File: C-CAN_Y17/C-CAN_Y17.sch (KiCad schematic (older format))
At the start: 19 parts, among them P3 CAN_Terminate, P4 MX150_8, P5 MX150_16, SW1 SW_Push, U1 MCP2551-I/SN, U2 AP1117, U3 Cypress_5LP, Y1 Crystal

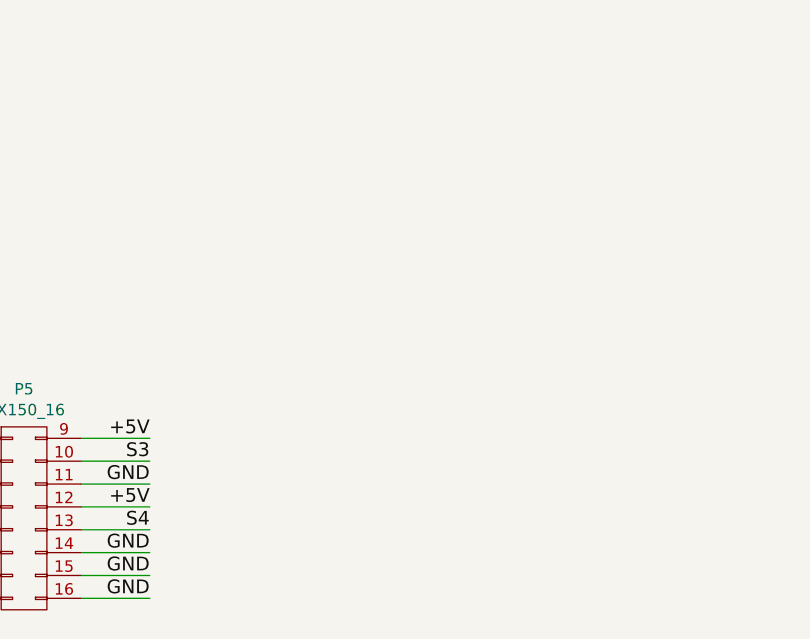
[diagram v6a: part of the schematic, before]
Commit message: C-CAN_Y17 Layout done, Oshpark DRC compliant
Still need to do the BOM but everything on the KiCAD side is complete
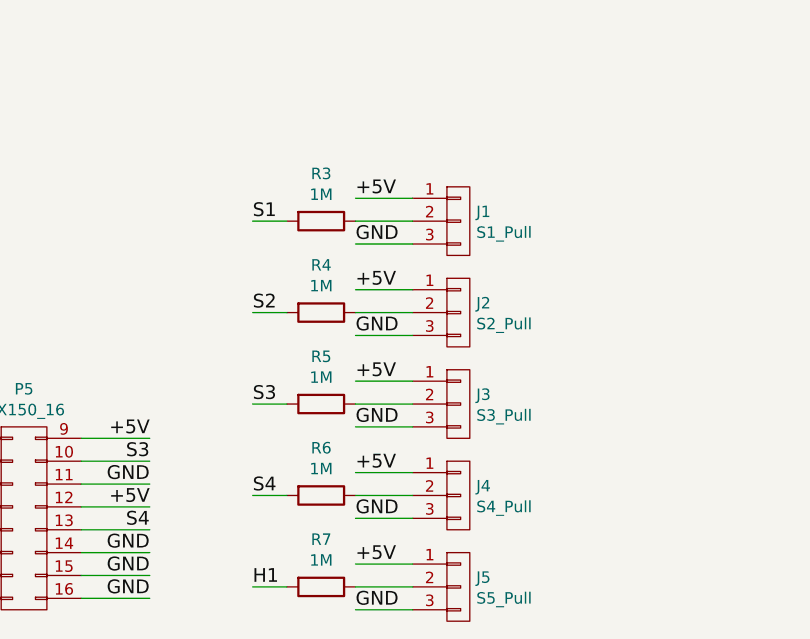
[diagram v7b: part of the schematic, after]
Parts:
- added J1: S1_Pull, Pin_Headers:Pin_Header_Straight_1x03_Pitch2.54mm, symbol CONN_01X03
- added J2: S2_Pull, Pin_Headers:Pin_Header_Straight_1x03_Pitch2.54mm, symbol CONN_01X03
- added J3: S3_Pull, Pin_Headers:Pin_Header_Straight_1x03_Pitch2.54mm, symbol CONN_01X03
- added J4: S4_Pull, Pin_Headers:Pin_Header_Straight_1x03_Pitch2.54mm, symbol CONN_01X03
- added J5: S5_Pull, Pin_Headers:Pin_Header_Straight_1x03_Pitch2.54mm, symbol CONN_01X03
- added R3, R4, R5, R6, R7: 1M, Resistors_SMD:R_0805_HandSoldering, symbol R
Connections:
- net +5V: now also J1.1 (P1), J2.1 (P1), J3.1 (P1), J4.1 (P1), J5.1 (P1)
- net GND: now also J1.3 (P3), J2.3 (P3), J3.3 (P3), J4.3 (P3), J5.3 (P3)
- net H1: now also R7.2
- net S1: now also R3.2
- net S2: now also R4.2
- net S3: now also R5.2
- net S4: now also R6.2
- new net: J1.2 (P2), R3.1
- new net: J2.2 (P2), R4.1
- new net: J3.2 (P2), R5.1
- new net: J4.2 (P2), R6.1
- new net: J5.2 (P2), R7.1
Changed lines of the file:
@@
 $EndComp
 Connection ~ 2700 1450
+$Comp
+L CONN_01X03 J1
+U 1 1 58BF3A96
+P 5300 5150
+F 0 "J1" H 5378 5191 50  0000 L CNN
+F 1 "S1_Pull" H 5378 5100 50  0000 L CNN
+F 2 "Pin_Headers:Pin_Header_Straight_1x03_Pitch2.54mm" H 850 -1250 50  0001 C CNN
+F 3 "" H 850 -1250 50  0001 C CNN
+	1    5300 5150
+	1    0    0    -1
+$EndComp
+$Comp
+L CONN_01X03 J2
+U 1 1 58BF3AFC
+P 5300 5550
+F 0 "J2" H 5378 5591 50  0000 L CNN
+F 1 "S2_Pull" H 5378 5500 50  0000 L CNN
+F 2 "Pin_Headers:Pin_Header_Straight_1x03_Pitch2.54mm" H 0   0   50  0001 C CNN
+F 3 "" H 0   0   50  0001 C CNN
+	1    5300 5550
+	1    0    0    -1
+$EndComp
+$Comp
+L CONN_01X03 J3
+U 1 1 58BF3B4E
+P 5300 5950
+F 0 "J3" H 5378 5991 50  0000 L CNN
+F 1 "S3_Pull" H 5378 5900 50  0000 L CNN
+F 2 "Pin_Headers:Pin_Header_Straight_1x03_Pitch2.54mm" H 50  0   50  0001 C CNN
+F 3 "" H 50  0   50  0001 C CNN
+	1    5300 5950
+	1    0    0    -1
+$EndComp
+$Comp
+L CONN_01X03 J4
+U 1 1 58BF3BA4
+P 5300 6350
+F 0 "J4" H 5378 6391 50  0000 L CNN
+F 1 "S4_Pull" H 5378 6300 50  0000 L CNN
+F 2 "Pin_Headers:Pin_Header_Straight_1x03_Pitch2.54mm" H 0   -50 50  0001 C CNN
+F 3 "" H 0   -50 50  0001 C CNN
+	1    5300 6350
+	1    0    0    -1
+$EndComp
+$Comp
+L CONN_01X03 J5
+U 1 1 58BF3BFC
+P 5300 6750
+F 0 "J5" H 5378 6791 50  0000 L CNN
+F 1 "S5_Pull" H 5378 6700 50  0000 L CNN
+F 2 "Pin_Headers:Pin_Header_Straight_1x03_Pitch2.54mm" H 0   -50 50  0001 C CNN
+F 3 "" H 0   -50 50  0001 C CNN
+	1    5300 6750
+	1    0    0    -1
+$EndComp
+Text Label 4850 5050 0    60   ~ 0
++5V
+Text Label 4850 5450 0    60   ~ 0
++5V
+Text Label 4850 5850 0    60   ~ 0
++5V
+Text Label 4850 6250 0    60   ~ 0
++5V
+Text Label 4850 6650 0    60   ~ 0
++5V
+Text Label 4850 5250 0    60   ~ 0
+GND
+Text Label 4850 5650 0    60   ~ 0
+GND
+Text Label 4850 6050 0    60   ~ 0
+GND
+Text Label 4850 6450 0    60   ~ 0
+GND
+Text Label 4850 6850 0    60   ~ 0
+GND
+Text Label 4400 5150 0    60   ~ 0
+S1
+Text Label 4400 5550 0    60   ~ 0
+S2
+Text Label 4400 5950 0    60   ~ 0
+S3
+Text Label 4400 6350 0    60   ~ 0
+S4
+Text Label 4400 6750 0    60   ~ 0
+H1
+$Comp
+L R R3
+U 1 1 58BF40AB
+P 4700 5150
+F 0 "R3" V 4493 5150 50  0000 C CNN
+F 1 "1M" V 4584 5150 50  0000 C CNN
+F 2 "Resistors_SMD:R_0805_HandSoldering" V 630 -350 50  0001 C CNN
+F 3 "" H 700 -350 50  0001 C CNN
+	1    4700 5150
+	0    1    1    0
+$EndComp
+$Comp
+L R R4
+U 1 1 58BF4147
+P 4700 5550
+F 0 "R4" V 4493 5550 50  0000 C CNN
+F 1 "1M" V 4584 5550 50  0000 C CNN
+F 2 "Resistors_SMD:R_0805_HandSoldering" V 130 0   50  0001 C CNN
+F 3 "" H 200 0   50  0001 C CNN
+	1    4700 5550
+	0    1    1    0
+$EndComp
+$Comp
+L R R5
+U 1 1 58BF41C2
+P 4700 5950
+F 0 "R5" V 4493 5950 50  0000 C CNN
+F 1 "1M" V 4584 5950 50  0000 C CNN
+F 2 "Resistors_SMD:R_0805_HandSoldering" V 130 0   50  0001 C CNN
+F 3 "" H 200 0   50  0001 C CNN
+	1    4700 5950
+	0    1    1    0
+$EndComp
+$Comp
+L R R6
+U 1 1 58BF42C4
+P 4700 6350
+F 0 "R6" V 4493 6350 50  0000 C CNN
+F 1 "1M" V 4584 6350 50  0000 C CNN
+F 2 "Resistors_SMD:R_0805_HandSoldering" V 130 0   50  0001 C CNN
+F 3 "" H 200 0   50  0001 C CNN
+	1    4700 6350
+	0    1    1    0
+$EndComp
+$Comp
+L R R7
+U 1 1 58BF4345
+P 4700 6750
+F 0 "R7" V 4493 6750 50  0000 C CNN
+F 1 "1M" V 4584 6750 50  0000 C CNN
+F 2 "Resistors_SMD:R_0805_HandSoldering" V 130 0   50  0001 C CNN
+F 3 "" H 200 0   50  0001 C CNN
+	1    4700 6750
+	0    1    1    0
+$EndComp
+Wire Wire Line
+	4400 5150 4550 5150
+Wire Wire Line
+	4400 5550 4550 5550
+Wire Wire Line
+	4400 5950 4550 5950
+Wire Wire Line
+	4400 6350 4550 6350
+Wire Wire Line
+	4400 6750 4550 6750
+Wire Wire Line
+	4850 5150 5100 5150
+Wire Wire Line
+	4850 5050 5100 5050
+Wire Wire Line
+	4850 5250 5100 5250
+Wire Wire Line
+	4850 5450 5100 5450
+Wire Wire Line
+	4850 5550 5100 5550
+Wire Wire Line
+	4850 5650 5100 5650
+Wire Wire Line
+	4850 5850 5100 5850
+Wire Wire Line
+	4850 5950 5100 5950
+Wire Wire Line
+	4850 6050 5100 6050
+Wire Wire Line
+	4850 6250 5100 6250
+Wire Wire Line
+	4850 6350 5100 6350
+Wire Wire Line
+	4850 6450 5100 6450
+Wire Wire Line
+	4850 6650 5100 6650
+Wire Wire Line
+	4850 6750 5100 6750
+Wire Wire Line
+	4850 6850 5100 6850
 $EndSCHEMATC

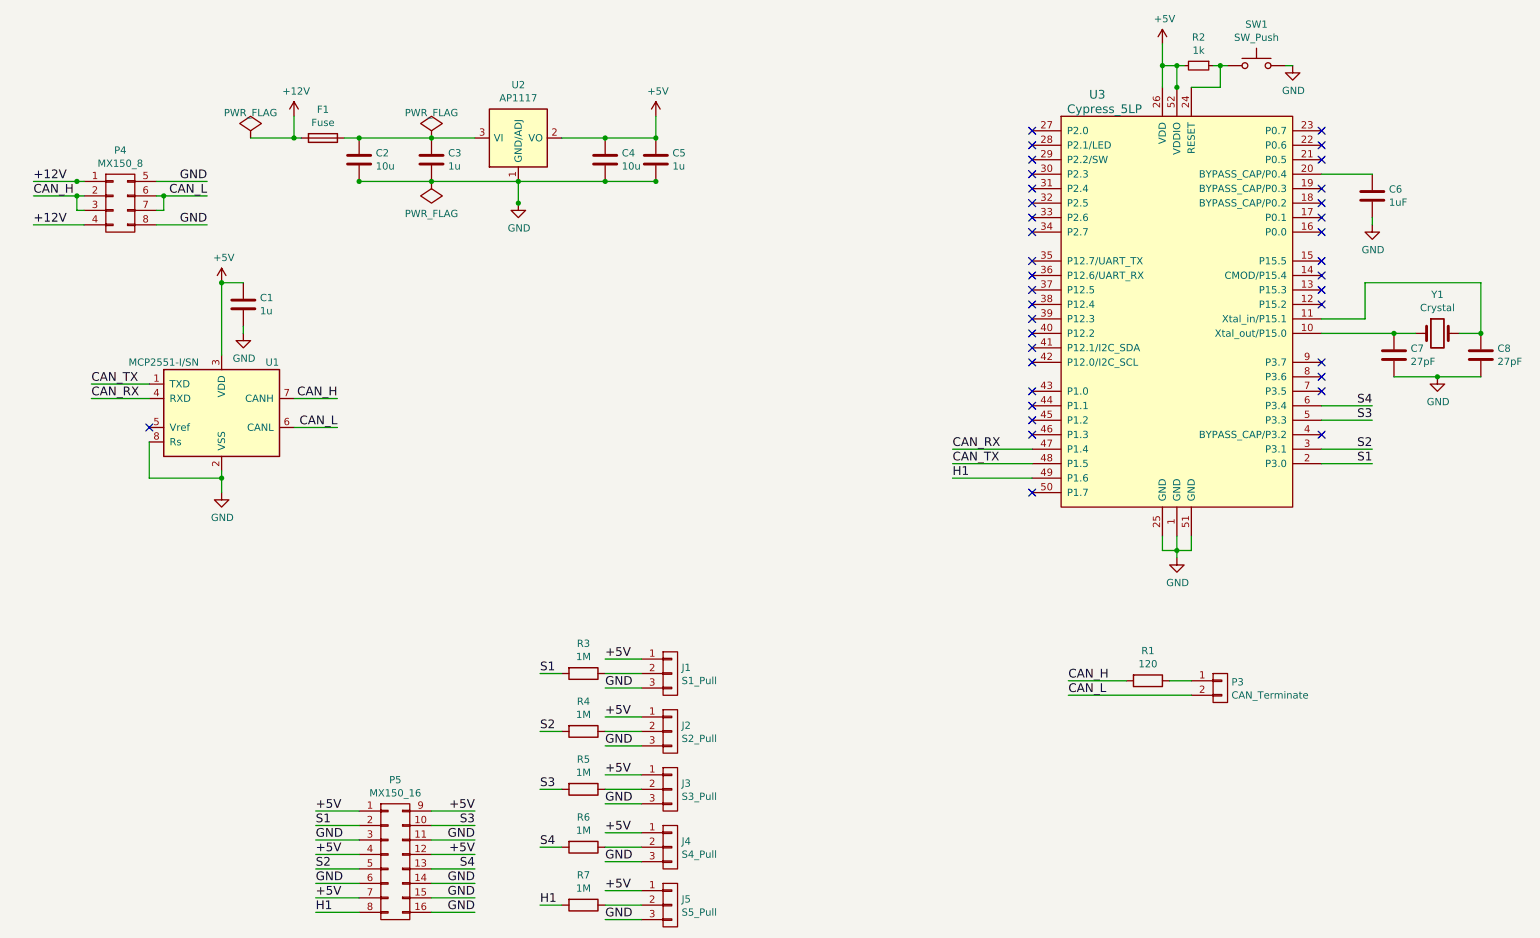
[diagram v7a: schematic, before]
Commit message: Added a bunch of step export files, some solidworks too for the C-CAN_Y17 Enclosure
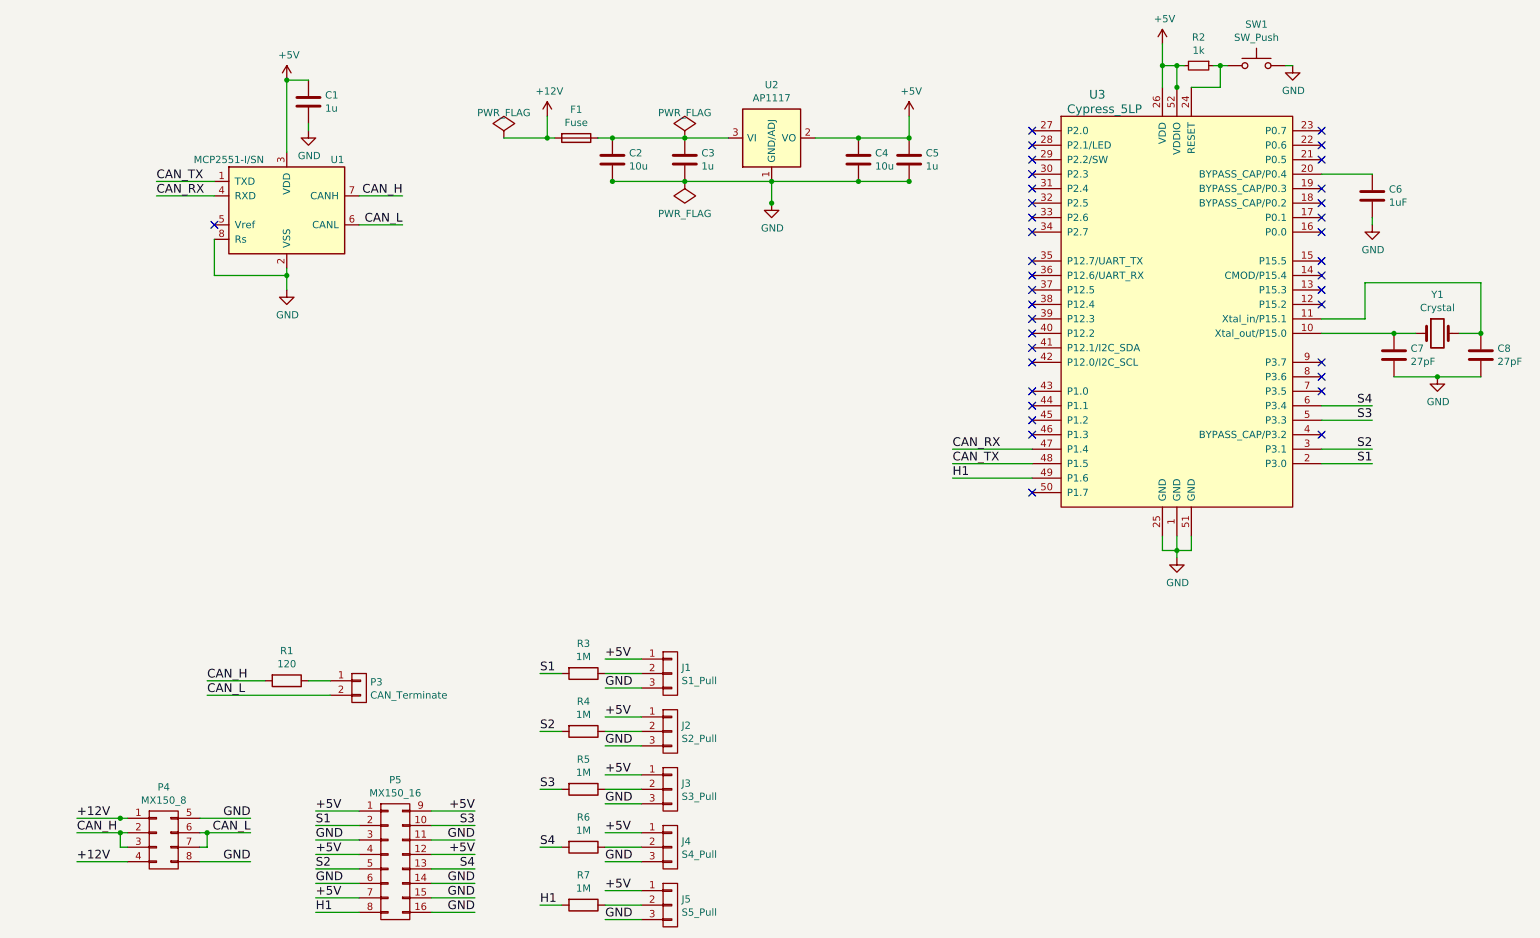
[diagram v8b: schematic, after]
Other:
- moved on the sheet: C1, C2, C3, C4, C5, F1, P3, P4, R1, U1, U2
